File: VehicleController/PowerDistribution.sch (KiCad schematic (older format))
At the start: 21 parts, among them P2 RPi_USB_PWR, U6 TL431, U7 BTS6133D, U8 R-78E5.0-1.0

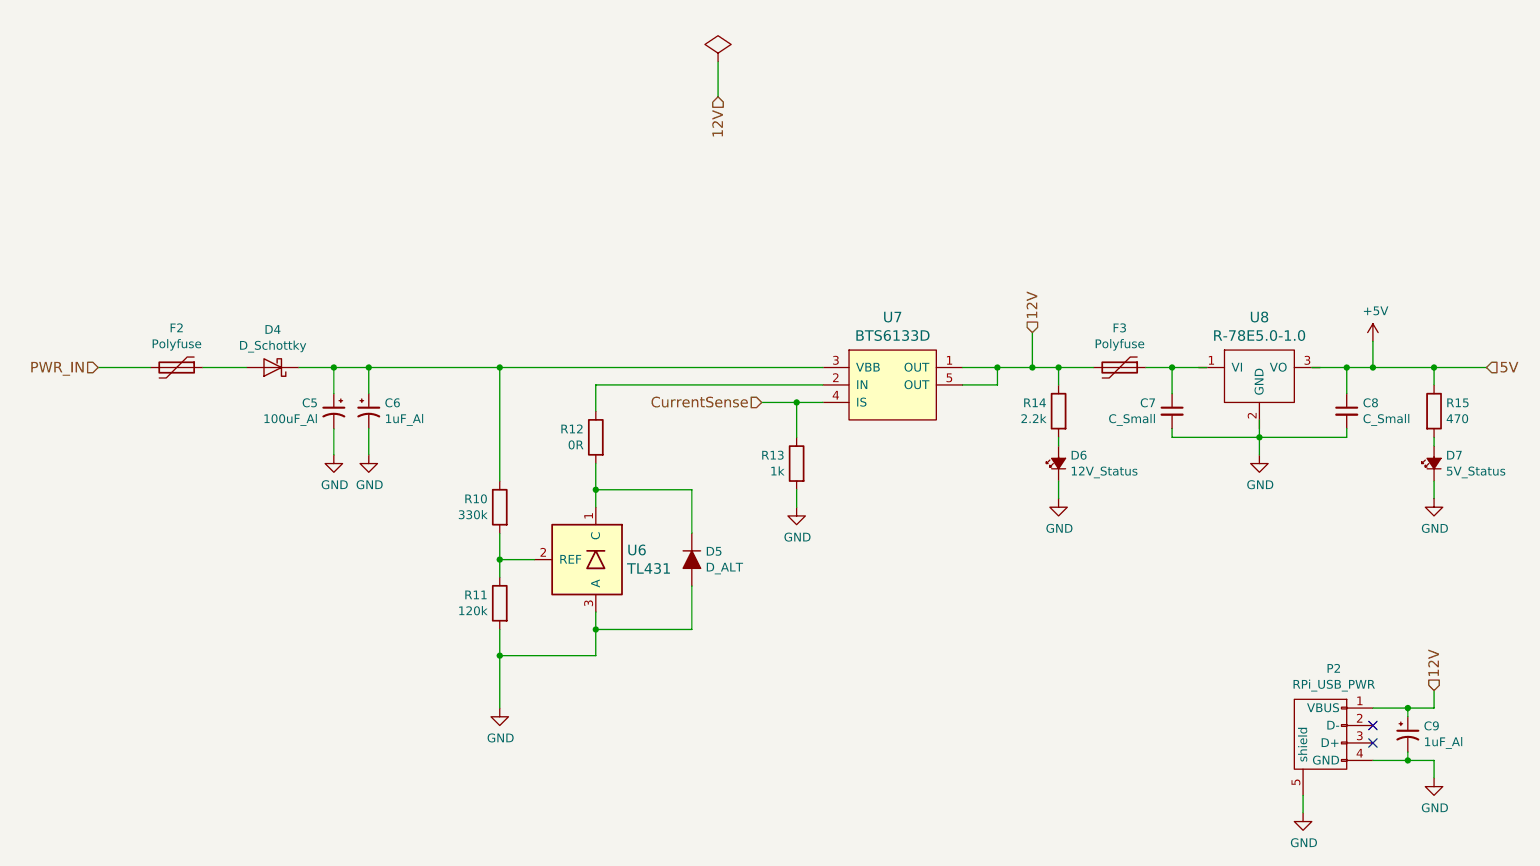
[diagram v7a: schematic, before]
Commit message: Finish VCU schematic, most footprint selections.  Start layout
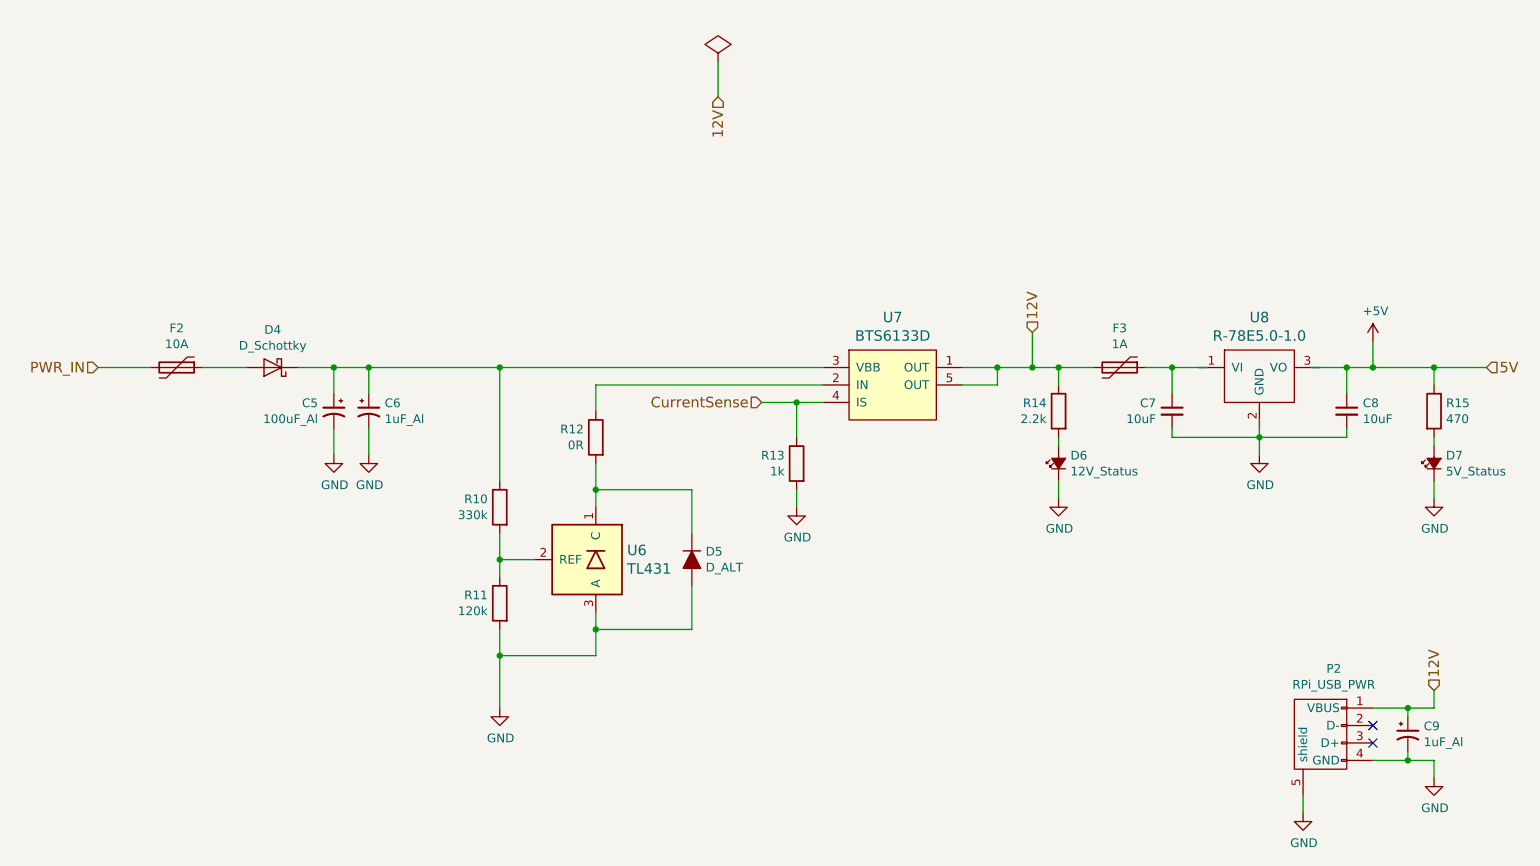
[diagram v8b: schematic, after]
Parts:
- C5: footprint (none) -> Capacitors_SMD:c_elec_6.3x7.7
- C6: footprint (none) -> Capacitors_SMD:c_elec_4x4.5
- C7, C8: value C_Small -> 10uF; footprint (none) -> Capacitors_SMD:C_0805_HandSoldering
- C9: footprint (none) -> Capacitors_SMD:c_elec_4x5.3
- D4, D5: footprint (none) -> Diodes_SMD:SMA_Handsoldering
- D6, D7: footprint (none) -> LEDs:LED-0805
- F2: value Polyfuse -> 10A
- F3: value Polyfuse -> 1A; footprint (none) -> Fuse_Holders_and_Fuses:Fuse_SMD1206_HandSoldering
- P2: footprint (none) -> UNCAMotorsports:USB-A-THT
- R10, R11, R12, R13, R14, R15: footprint (none) -> Resistors_SMD:R_0805_HandSoldering
- U6: footprint (none) -> TO_SOT_Packages_SMD:SOT-23_Handsoldering
- U7: footprint (none) -> UNCAMotorsports:TO-252-5
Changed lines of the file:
@@
 encoding utf-8
 Sheet 2 5
-Title ""
-Date ""
-Rev ""
-Comp ""
+Title "Vehicle Controller"
+Date "2017-03-11"
+Rev "001"
+Comp "UNC Asheville Motorsports"
 Comment1 ""
 Comment2 ""
@@
 F 0 "D4" H 3000 2534 50  0000 C CNN
 F 1 "D_Schottky" H 3000 2625 50  0000 C CNN
-F 2 "" H 3000 2750 50  0000 C CNN
+F 2 "Diodes_SMD:SMA_Handsoldering" H 3000 2750 50  0001 C CNN
 F 3 "" H 3000 2750 50  0000 C CNN
 	1    3000 2750
@@
 P 2450 2750
 F 0 "F2" V 2225 2750 50  0000 C CNN
-F 1 "Polyfuse" V 2316 2750 50  0000 C CNN
+F 1 "10A" V 2316 2750 50  0000 C CNN
 F 2 "" H 2500 2550 50  0001 L CNN
 F 3 "" H 2450 2750 50  0001 C CNN
@@
 F 0 "U6" H 4671 3903 60  0000 R CNN
 F 1 "TL431" H 4671 3797 60  0000 R CNN
-F 2 "" H 4850 3800 60  0000 C CNN
+F 2 "TO_SOT_Packages_SMD:SOT-23_Handsoldering" H 4850 3800 60  0001 C CNN
 F 3 "" H 4850 3800 60  0000 C CNN
 	1    4850 3850
@@
 F 0 "U7" H 6550 3237 60  0000 C CNN
 F 1 "BTS6133D" H 6550 3131 60  0000 C CNN
-F 2 "" H 6700 3050 60  0000 C CNN
+F 2 "UNCAMotorsports:TO-252-5" H 6700 3050 60  0001 C CNN
 F 3 "" H 6700 3050 60  0000 C CNN
 	1    6550 2850
@@
 F 0 "R10" H 4369 3596 50  0000 L CNN
 F 1 "330k" H 4369 3505 50  0000 L CNN
-F 2 "" V 4230 3550 50  0000 C CNN
+F 2 "Resistors_SMD:R_0805_HandSoldering" V 4230 3550 50  0001 C CNN
 F 3 "" H 4300 3550 50  0000 C CNN
 	1    4300 3550
@@
 F 0 "R11" H 4369 4146 50  0000 L CNN
 F 1 "120k" H 4369 4055 50  0000 L CNN
-F 2 "" V 4230 4100 50  0000 C CNN
+F 2 "Resistors_SMD:R_0805_HandSoldering" V 4230 4100 50  0001 C CNN
 F 3 "" H 4300 4100 50  0000 C CNN
 	1    4300 4100
@@
 F 0 "R13" H 6069 3346 50  0000 L CNN
 F 1 "1k" H 6069 3255 50  0000 L CNN
-F 2 "" V 5930 3300 50  0000 C CNN
+F 2 "Resistors_SMD:R_0805_HandSoldering" V 5930 3300 50  0001 C CNN
 F 3 "" H 6000 3300 50  0000 C CNN
 	1    6000 3300
@@
 $EndComp
 $Comp
-L GND #PWR29
+L GND #PWR028
 U 1 1 587C7BE3
 P 6000 3550
-F 0 "#PWR29" H 6000 3300 50  0001 C CNN
+F 0 "#PWR028" H 6000 3300 50  0001 C CNN
 F 1 "GND" H 6005 3377 50  0000 C CNN
 F 2 "" H 6000 3550 50  0000 C CNN
@@
 $EndComp
 $Comp
-L GND #PWR28
+L GND #PWR029
 U 1 1 587C7BF7
 P 4300 4700
-F 0 "#PWR28" H 4300 4450 50  0001 C CNN
+F 0 "#PWR029" H 4300 4450 50  0001 C CNN
 F 1 "GND" H 4305 4527 50  0000 C CNN
 F 2 "" H 4300 4700 50  0000 C CNN
@@
 P 8150 3000
 F 0 "C7" H 8242 3046 50  0000 L CNN
-F 1 "C_Small" H 8242 2955 50  0000 L CNN
-F 2 "" H 8150 3000 50  0000 C CNN
+F 1 "10uF" H 8242 2955 50  0000 L CNN
+F 2 "Capacitors_SMD:C_0805_HandSoldering" H 8150 3000 50  0001 C CNN
 F 3 "" H 8150 3000 50  0000 C CNN
 	1    8150 3000
@@
 P 9150 3000
 F 0 "C8" H 9242 3046 50  0000 L CNN
-F 1 "C_Small" H 9242 2955 50  0000 L CNN
-F 2 "" H 9150 3000 50  0000 C CNN
+F 1 "10uF" H 9242 2955 50  0000 L CNN
+F 2 "Capacitors_SMD:C_0805_HandSoldering" H 9150 3000 50  0001 C CNN
 F 3 "" H 9150 3000 50  0000 C CNN
 	1    9150 3000
@@
 $EndComp
 $Comp
-L GND #PWR31
+L GND #PWR030
 U 1 1 58AEB860
 P 8650 3250
-F 0 "#PWR31" H 8650 3000 50  0001 C CNN
+F 0 "#PWR030" H 8650 3000 50  0001 C CNN
 F 1 "GND" H 8655 3077 50  0000 C CNN
 F 2 "" H 8650 3250 50  0000 C CNN
@@
 5V
 $Comp
-L PWR_FLAG #FLG3
+L PWR_FLAG #FLG031
 U 1 1 58AF2028
 P 5550 1000
-F 0 "#FLG3" H 5550 1095 50  0001 C CNN
+F 0 "#FLG031" H 5550 1095 50  0001 C CNN
 F 1 "PWR_FLAG" H 5550 1224 50  0001 C CNN
 F 2 "" H 5550 1000 50  0000 C CNN
@@
 F 0 "P2" V 8575 4824 50  0000 C CNN
 F 1 "RPi_USB_PWR" V 8666 4824 50  0000 C CNN
-F 2 "" V 8950 4800 50  0000 C CNN
+F 2 "UNCAMotorsports:USB-A-THT" V 8950 4800 50  0001 C CNN
 F 3 "" V 8950 4800 50  0000 C CNN
 	1    9000 4900
@@
 $EndComp
 $Comp
-L GND #PWR32
+L GND #PWR032
 U 1 1 58B30D9F
 P 8900 5300
-F 0 "#PWR32" H 8900 5050 50  0001 C CNN
+F 0 "#PWR032" H 8900 5050 50  0001 C CNN
 F 1 "GND" H 8905 5127 50  0000 C CNN
 F 2 "" H 8900 5300 50  0000 C CNN
@@
 12V
 $Comp
-L GND #PWR35
+L GND #PWR033
 U 1 1 58B31164
 P 9650 5100
-F 0 "#PWR35" H 9650 4850 50  0001 C CNN
+F 0 "#PWR033" H 9650 4850 50  0001 C CNN
 F 1 "GND" H 9655 4927 50  0000 C CNN
 F 2 "" H 9650 5100 50  0000 C CNN
@@
 $EndComp
 $Comp
-L GND #PWR26
+L GND #PWR034
 U 1 1 58B0EFE3
 P 3350 3250
-F 0 "#PWR26" H 3350 3000 50  0001 C CNN
+F 0 "#PWR034" H 3350 3000 50  0001 C CNN
 F 1 "GND" H 3355 3077 50  0000 C CNN
 F 2 "" H 3350 3250 50  0000 C CNN
@@
 $EndComp
 $Comp
-L GND #PWR27
+L GND #PWR035
 U 1 1 58B0F09D
 P 3550 3250
-F 0 "#PWR27" H 3550 3000 50  0001 C CNN
+F 0 "#PWR035" H 3550 3000 50  0001 C CNN
 F 1 "GND" H 3555 3077 50  0000 C CNN
 F 2 "" H 3550 3250 50  0000 C CNN
@@
 F 0 "D5" V 5354 3929 50  0000 L CNN
 F 1 "D_ALT" V 5445 3929 50  0000 L CNN
-F 2 "" H 5400 3850 50  0000 C CNN
+F 2 "Diodes_SMD:SMA_Handsoldering" H 5400 3850 50  0001 C CNN
 F 3 "" H 5400 3850 50  0000 C CNN
 	1    5400 3850
@@
 	4850 3300 4850 3550
 $Comp
-L +5V #PWR33
+L +5V #PWR036
 U 1 1 58BE7A1A
 P 9300 2600
-F 0 "#PWR33" H 9350 2650 50  0001 C CNN
+F 0 "#PWR036" H 9350 2650 50  0001 C CNN
 F 1 "+5V" H 9315 2773 50  0000 C CNN
 F 2 "" H 550 -100 50  0001 C CNN
@@
 P 7850 2750
 F 0 "F3" V 7625 2750 50  0000 C CNN
-F 1 "Polyfuse" V 7716 2750 50  0000 C CNN
-F 2 "" H 7900 2550 50  0001 L CNN
+F 1 "1A" V 7716 2750 50  0000 C CNN
+F 2 "Fuse_Holders_and_Fuses:Fuse_SMD1206_HandSoldering" H 7900 2550 50  0001 L CNN
 F 3 "" H 7850 2750 50  0001 C CNN
 	1    7850 2750
@@
 F 0 "R14" H 7569 3046 50  0000 L CNN
 F 1 "2.2k" H 7569 2955 50  0000 L CNN
-F 2 "" V 7430 3000 50  0000 C CNN
+F 2 "Resistors_SMD:R_0805_HandSoldering" V 7430 3000 50  0001 C CNN
 F 3 "" H 7500 3000 50  0000 C CNN
 	1    7500 3000
@@
 F 0 "D6" V 7546 3232 50  0000 R CNN
 F 1 "12V_Status" V 7455 3232 50  0000 R CNN
-F 2 "" V 750 -300 50  0001 C CNN
+F 2 "LEDs:LED-0805" V 750 -300 50  0001 C CNN
 F 3 "" V 750 -300 50  0001 C CNN
 	1    7500 3300
@@
 Connection ~ 7500 2750
 $Comp
-L GND #PWR30
+L GND #PWR037
 U 1 1 58C31B60
 P 7500 3500
-F 0 "#PWR30" H 7500 3250 50  0001 C CNN
+F 0 "#PWR037" H 7500 3250 50  0001 C CNN
 F 1 "GND" H 7505 3327 50  0000 C CNN
 F 2 "" H 7500 3500 50  0000 C CNN
@@
 F 0 "D7" V 9696 3232 50  0000 R CNN
 F 1 "5V_Status" V 9605 3232 50  0000 R CNN
-F 2 "" V 2900 -300 50  0001 C CNN
+F 2 "LEDs:LED-0805" V 2900 -300 50  0001 C CNN
 F 3 "" V 2900 -300 50  0001 C CNN
 	1    9650 3300
@@
 F 0 "R15" H 9719 3046 50  0000 L CNN
 F 1 "470" H 9719 2955 50  0000 L CNN
-F 2 "" V 9580 3000 50  0000 C CNN
+F 2 "Resistors_SMD:R_0805_HandSoldering" V 9580 3000 50  0001 C CNN
 F 3 "" H 9650 3000 50  0000 C CNN
 	1    9650 3000
@@
 	9650 3200 9650 3150
 $Comp
-L GND #PWR34
+L GND #PWR038
 U 1 1 58C32364
 P 9650 3500
-F 0 "#PWR34" H 9650 3250 50  0001 C CNN
+F 0 "#PWR038" H 9650 3250 50  0001 C CNN
 F 1 "GND" H 9655 3327 50  0000 C CNN
 F 2 "" H 9650 3500 50  0000 C CNN
@@
 F 0 "C5" H 3441 3046 50  0000 L CNN
 F 1 "100uF_Al" H 3441 2955 50  0000 L CNN
-F 2 "" H 700 -350 50  0001 C CNN
+F 2 "Capacitors_SMD:c_elec_6.3x7.7" H 700 -350 50  0001 C CNN
 F 3 "" H 700 -350 50  0001 C CNN
 	1    3350 3000
@@
 F 0 "C6" H 3641 3046 50  0000 L CNN
 F 1 "1uF_Al" H 3641 2955 50  0000 L CNN
-F 2 "" H 900 -350 50  0001 C CNN
+F 2 "Capacitors_SMD:c_elec_4x4.5" H 900 -350 50  0001 C CNN
 F 3 "" H 900 -350 50  0001 C CNN
 	1    3550 3000
@@
 F 0 "R12" H 4919 3196 50  0000 L CNN
 F 1 "0R" H 4919 3105 50  0000 L CNN
-F 2 "" V 4780 3150 50  0000 C CNN
+F 2 "Resistors_SMD:R_0805_HandSoldering" V 4780 3150 50  0001 C CNN
 F 3 "" H 4850 3150 50  0000 C CNN
 	1    4850 3150
@@
 F 0 "U8" H 8650 3037 60  0000 C CNN
 F 1 "R-78E5.0-1.0" H 8650 2931 60  0000 C CNN
-F 2 "" H 2600 1150 60  0000 C CNN
+F 2 "" H 2600 1150 60  0001 C CNN
 F 3 "" H 2600 1150 60  0000 C CNN
 	1    8650 2750
@@
 F 0 "C9" H 9591 4896 50  0000 L CNN
 F 1 "1uF_Al" H 9591 4805 50  0000 L CNN
-F 2 "" H 0   0   50  0001 C CNN
+F 2 "Capacitors_SMD:c_elec_4x5.3" H 0   0   50  0001 C CNN
 F 3 "" H 0   0   50  0001 C CNN
 	1    9500 4850
